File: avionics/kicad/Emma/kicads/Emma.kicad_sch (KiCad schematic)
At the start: 74 parts, among them U1 ByA 100nF +3V3 U1-VDDA Bypass, U1 ByB 100nF +3V3 U1-VDD Bypass

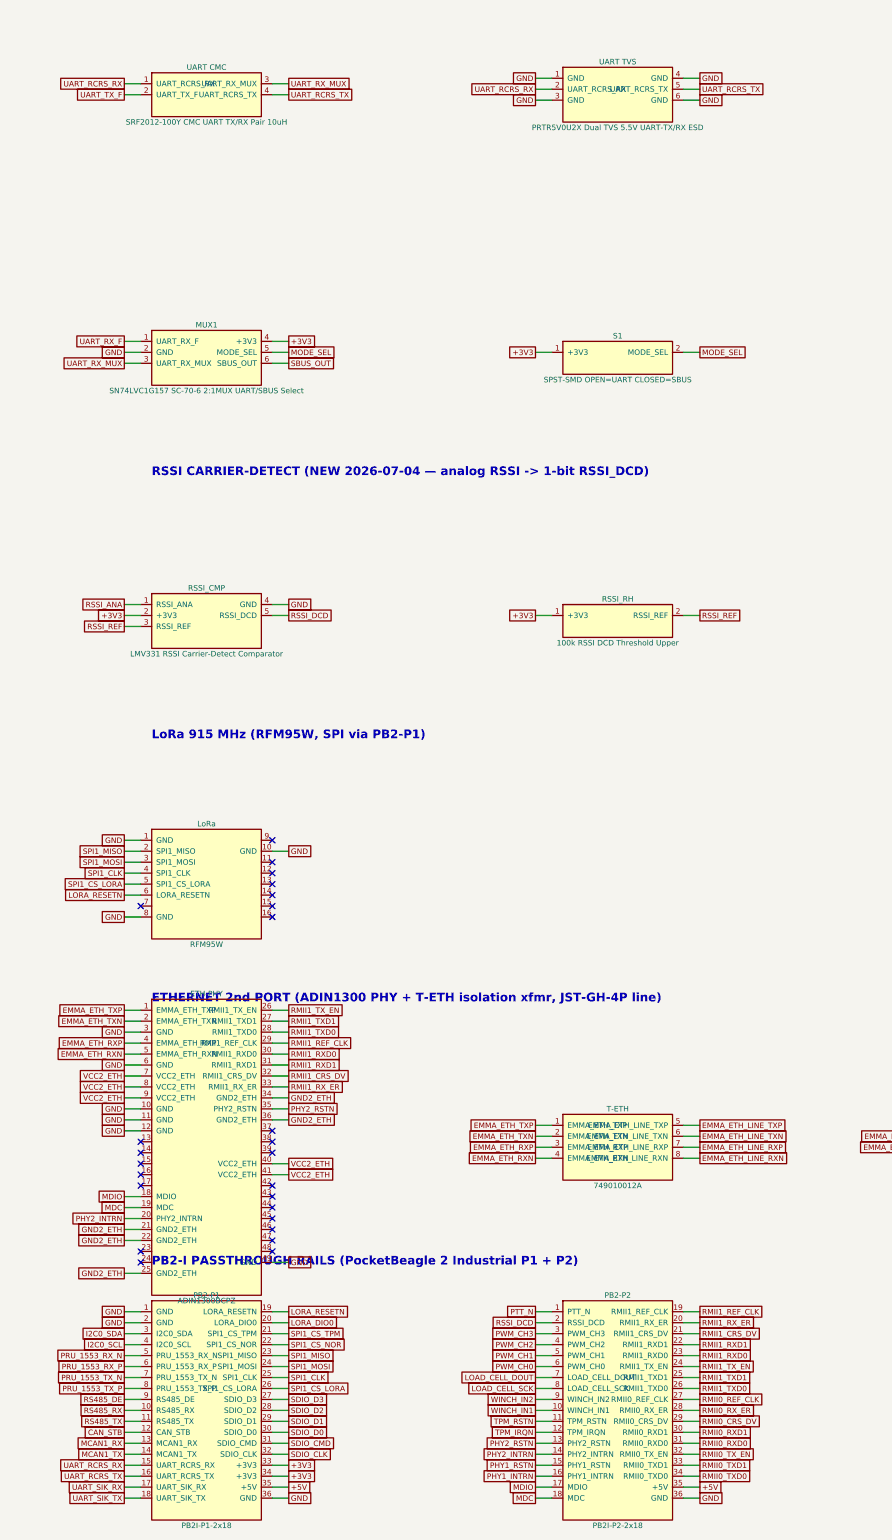
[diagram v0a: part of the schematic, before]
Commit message: Resolve TODO 0.1: rename RCRS code identifiers to 49MHZ_XCVR/XCVR-49MHZ
Code (net labels, C macros, connector/config identifiers) previously used
"RCRS" as a naming convention under the mistaken assumption the 49 MHz
link falls under FCC Part 95 Radio Control Radio Service. It's actually
governed by 47 CFR Part 15 §15.235 (REF-FCC-003) -- Part 95 was evaluated
and rejected (REF-FCC-004). User-approved rename target is frequency-
qualified "49MHZ_XCVR"/"XCVR-49MHZ" to avoid ambiguity with "Emma," the
board name that also carries LoRa.

Renamed: SI5351_RCRS_*/si5351_set_rcrs_channel() and MAL_RCRS_* firmware
macros; UART_RCRS_TX/RX KiCad net labels in the Zoe/Emma schematics and
PCBs (pure net-name text substitution, occurrence counts verified 1:1,
no geometry/placement/routing touched) and their generator scripts;
RCRS-49/TVS-RCRS/FB-RCRS component naming in Emma.md/Zoe.md and the
active current-specification files; a DTS pinctrl label and a malcolm
config key.

While auditing, also found and corrected a stale/incorrect citation in
the Cape-B-2 DTS overlay and in serenity-rev-r.jsx that still cited
"47 CFR Part 95 ... RCRS" as the governing regulation for the 49 MHz
channel plan -- the exact claim REFERENCES.md's REF-FCC-003 documents
as superseded everywhere else. Corrected to cite Part 15 Section 15.235.

Left unchanged: legitimate regulatory-term uses of "RCRS" (correctly
discussing the real FCC Part 95 RCRS designation for comparison/
rejection purposes); dated historical WBS log entries; already-archived
BOM snapshots that self-document the same correction via strikethrough;
Gerber fab output (net-name text is informational, doesn't affect the
physical board); the rcrs49_wire_post.scad filename itself (a physical-
file rename touching 7+ cross-references is separate, larger work).

ERC/DRC could not be re-verified in this environment: tools/validate_kicad.py
requires KiCad >=8 (sch erc/pcb drc CLI subcommands); only KiCad 7.0.11
was installable here (both the Ki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
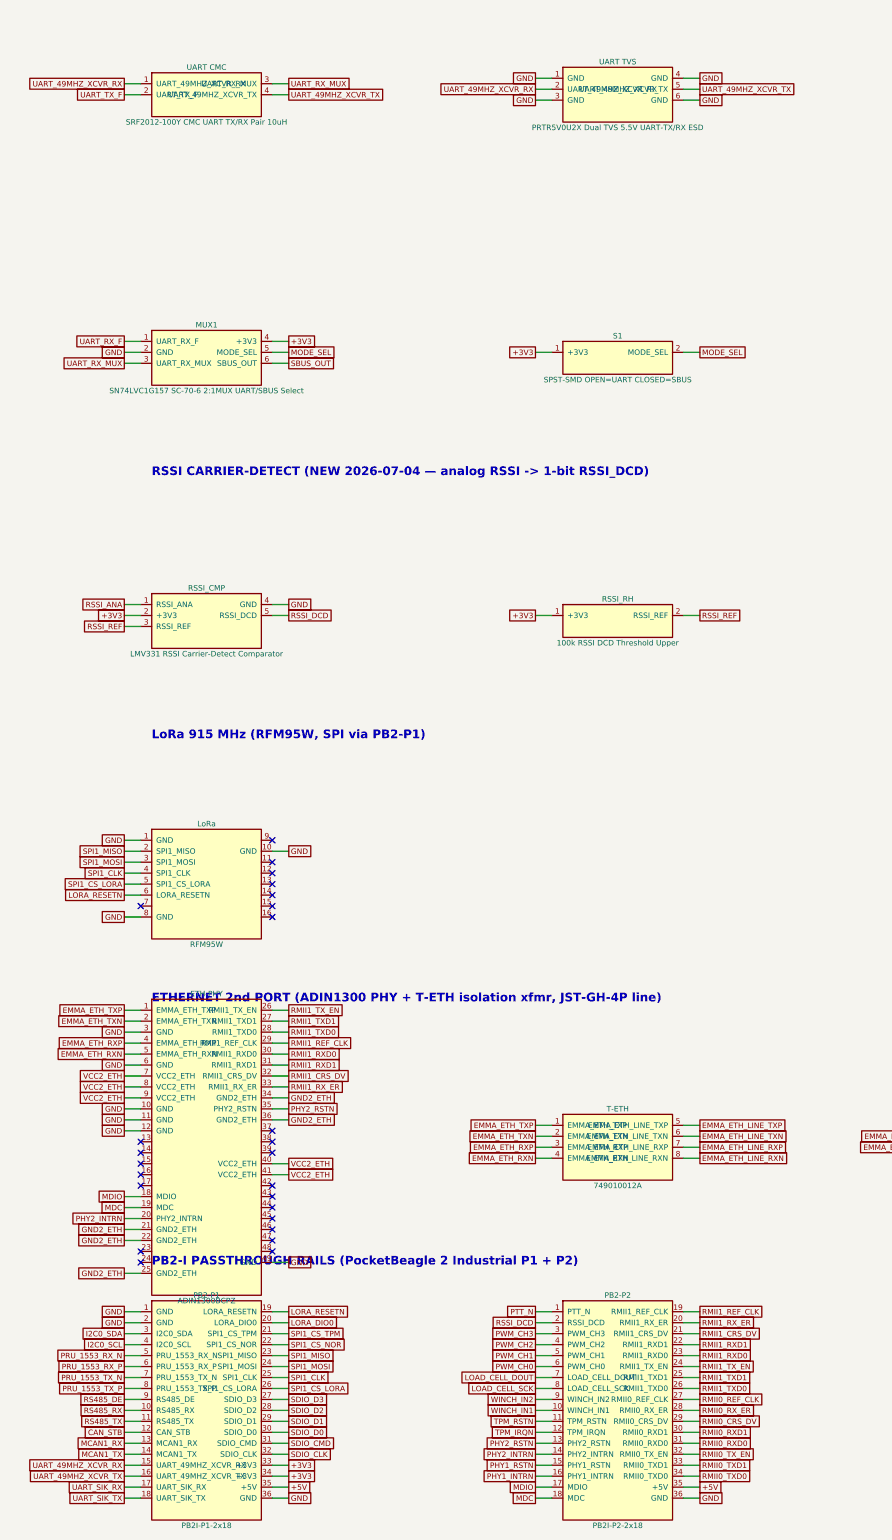
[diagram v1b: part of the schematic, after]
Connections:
- net UART_RCRS_RX renamed UART_49MHZ_XCVR_RX
- net UART_RCRS_TX renamed UART_49MHZ_XCVR_TX
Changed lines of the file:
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@@
   )
   (wire (pts (xy 48.26 731.52) (xy 44.45 731.52)) (stroke (width 0) (type default)))
-  (global_label "UART_RCRS_RX" (shape passive) (at 44.45 731.52 180) (effects (font (size 1.27 1.27)) (justify right)))
+  (global_label "UART_49MHZ_XCVR_RX" (shape passive) (at 44.45 731.52 180) (effects (font (size 1.27 1.27)) (justify right)))
   (wire (pts (xy 48.26 734.06) (xy 44.45 734.06)) (stroke (width 0) (type default)))
   (global_label "UART_TX_F" (shape passive) (at 44.45 734.06 180) (effects (font (size 1.27 1.27)) (justify right)))
@@
   (global_label "UART_RX_MUX" (shape passive) (at 82.55 731.52 0) (effects (font (size 1.27 1.27)) (justify left)))
   (wire (pts (xy 78.74 734.06) (xy 82.55 734.06)) (stroke (width 0) (type default)))
-  (global_label "UART_RCRS_TX" (shape passive) (at 82.55 734.06 0) (effects (font (size 1.27 1.27)) (justify left)))
+  (global_label "UART_49MHZ_XCVR_TX" (shape passive) (at 82.55 734.06 0) (effects (font (size 1.27 1.27)) (justify left)))
   (symbol (lib_id "S_UART_TVS") (at 158.75 734.06 0) (unit 1)
     (exclude_from_sim no) (in_bom yes) (on_board yes) (dnp no)
@@
   (global_label "GND" (shape passive) (at 139.70 730.25 180) (effects (font (size 1.27 1.27)) (justify right)))
   (wire (pts (xy 143.51 732.79) (xy 139.70 732.79)) (stroke (width 0) (type default)))
-  (global_label "UART_RCRS_RX" (shape passive) (at 139.70 732.79 180) (effects (font (size 1.27 1.27)) (justify right)))
+  (global_label "UART_49MHZ_XCVR_RX" (shape passive) (at 139.70 732.79 180) (effects (font (size 1.27 1.27)) (justify right)))
   (wire (pts (xy 143.51 735.33) (xy 139.70 735.33)) (stroke (width 0) (type default)))
   (global_label "GND" (shape passive) (at 139.70 735.33 180) (effects (font (size 1.27 1.27)) (justify right)))
@@
   (global_label "GND" (shape passive) (at 177.80 730.25 0) (effects (font (size 1.27 1.27)) (justify left)))
   (wire (pts (xy 173.99 732.79) (xy 177.80 732.79)) (stroke (width 0) (type default)))
-  (global_label "UART_RCRS_TX" (shape passive) (at 177.80 732.79 0) (effects (font (size 1.27 1.27)) (justify left)))
+  (global_label "UART_49MHZ_XCVR_TX" (shape passive) (at 177.80 732.79 0) (effects (font (size 1.27 1.27)) (justify left)))
   (wire (pts (xy 173.99 735.33) (xy 177.80 735.33)) (stroke (width 0) (type default)))
   (global_label "GND" (shape passive) (at 177.80 735.33 0) (effects (font (size 1.27 1.27)) (justify left)))
@@
   (global_label "MCAN1_TX" (shape passive) (at 44.45 1049.02 180) (effects (font (size 1.27 1.27)) (justify right)))
   (wire (pts (xy 48.26 1051.56) (xy 44.45 1051.56)) (stroke (width 0) (type default)))
-  (global_label "UART_RCRS_RX" (shape passive) (at 44.45 1051.56 180) (effects (font (size 1.27 1.27)) (justify right)))
+  (global_label "UART_49MHZ_XCVR_RX" (shape passive) (at 44.45 1051.56 180) (effects (font (size 1.27 1.27)) (justify right)))
   (wire (pts (xy 48.26 1054.10) (xy 44.45 1054.10)) (stroke (width 0) (type default)))
-  (global_label "UART_RCRS_TX" (shape passive) (at 44.45 1054.10 180) (effects (font (size 1.27 1.27)) (justify right)))
+  (global_label "UART_49MHZ_XCVR_TX" (shape passive) (at 44.45 1054.10 180) (effects (font (size 1.27 1.27)) (justify right)))
   (wire (pts (xy 48.26 1056.64) (xy 44.45 1056.64)) (stroke (width 0) (type default)))
   (global_label "UART_SIK_RX" (shape passive) (at 44.45 1056.64 180) (effects (font (size 1.27 1.27)) (justify right)))

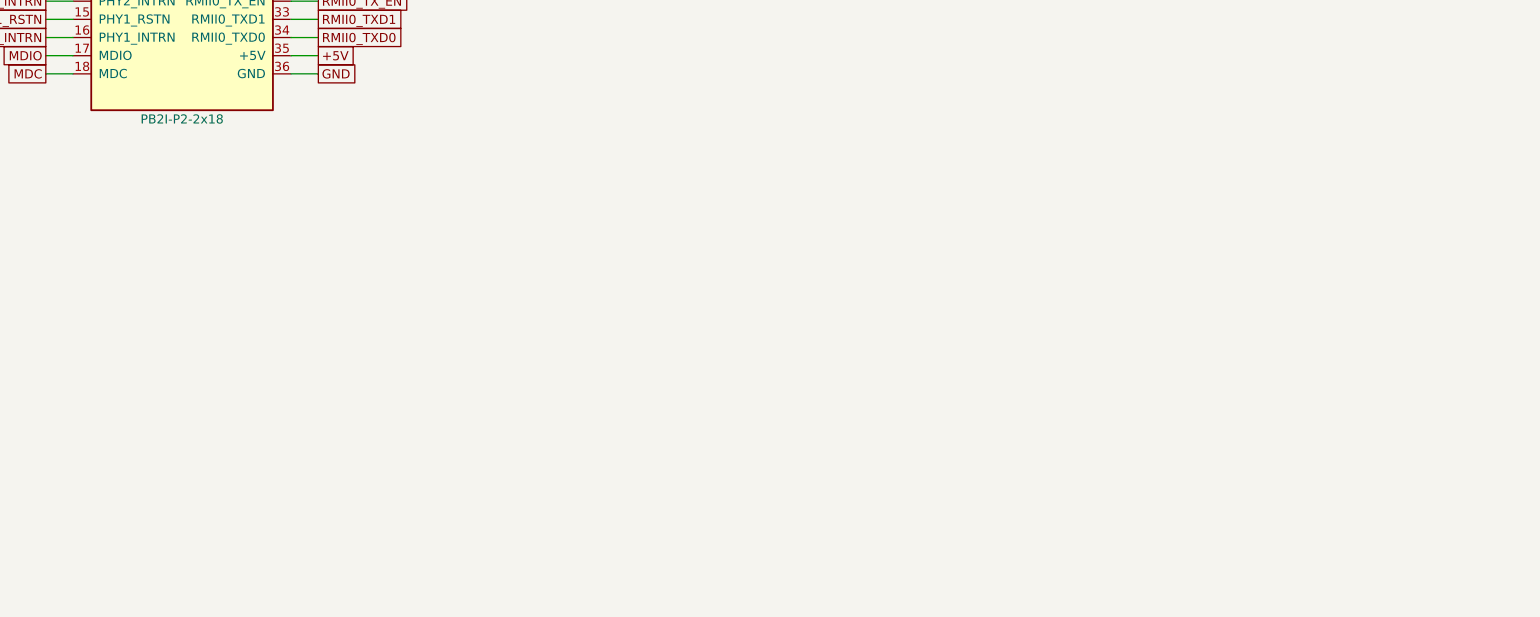
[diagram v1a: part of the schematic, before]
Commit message: Fleet trust module (MCU+TPM+isolated CAN-FD+RS-485) across new CAN-PERIPH-GW-1 board, Jayne, Kaylee, Emma; ISOW1412 swap on Wash/Zoë
- New stackable CAN-PERIPH-GW-1 gateway board (N_STACKS param): MSPM0G3507
  + SLB9670 TPM + ISOW1044BDFMR isolated CAN-FD + ISOW1412 isolated RS-485,
  informed by the public VimDrones ap_periph_pico/ESC S50 concept (no
  VimDrones GPL-3.0 source copied). PCB freerouted via the Specctra DSN/SES
  bridge (tools/export-specctra-dsn.py + import-specctra-ses.py +
  freerouting 2.2.4); user's manual footprint packing preserved.
- Jayne: added ISOW1412 isolated RS-485 (Section H); MSPM0G3507 pinmux
  re-verified against the real datasheet for all new assignments.
- Kaylee: full trust module added via non-destructive schematic injection
  (inject_kaylee_trust_module.py) -- gen_kaylee.py itself has drifted from
  the checked-in file and is not safe to regenerate from (tracked as an
  open item).
- Emma: SLB9670 TPM added via a dedicated header (inject_emma_tpm.py); no
  separate CAN/RS-485 needed, reaches the bus via Zoë's P1/P2 link.
- Fleet-wide ADM2795E -> ISOW1412 (integrated isolated DC-DC). While
  swapping Wash/Zoë, fixed their pre-existing broken ADM2795EBRWZ pin
  numbering and wrong ISOW1044BDFMR footprint (SOIC-16W on a 20-pin part).
- REFERENCES.md: REF-SENSOR-009/010/011 (ISOW1044/ISOW1412/SLB9670),
  ADM2795E supersession, Wash/Zoë defect history, vimdrones GPL note.
- WBS/TODO updated across avionics, airframe/wings-nacelles, and root:
  AK7455 nacelle tilt data is now bus-published by the gateway rather than
  read directly by River/Simon.

Co-Authored-By: Claude Sonnet 5 <noreply@anthropic.com>
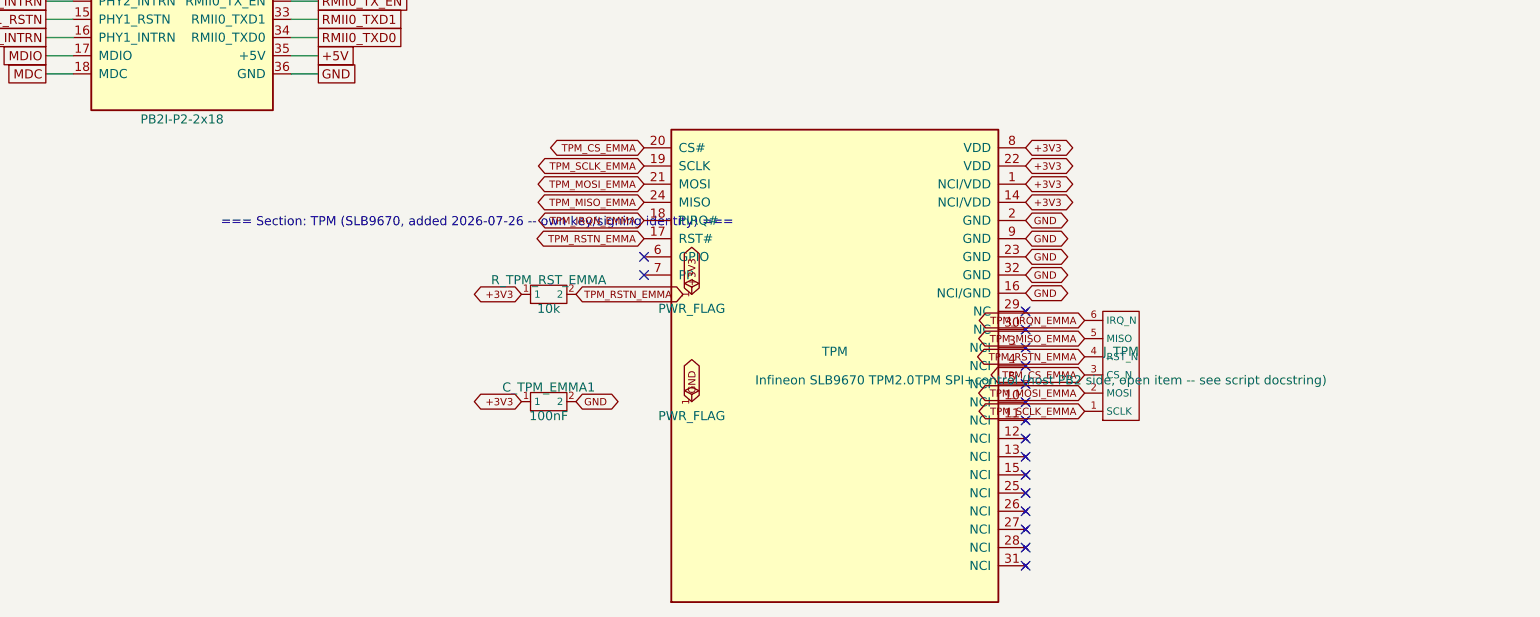
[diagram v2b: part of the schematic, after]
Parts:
- added C_TPM_EMMA1: 100nF, Capacitor_SMD:C_0402_1005Metric, symbol C_Generic_TPM
- added J_TPM: TPM SPI+control (host PB2 side, open item -- see 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, Connector_PinHeader_2.54mm:PinHeader_1x06_P2.54mm_Vertical, symbol J_TPM_EMMA
- added R_TPM_RST_EMMA: 10k, Resistor_SMD:R_0402_1005Metric, symbol R_Generic_TPM
- added TPM: Infineon SLB9670 TPM2.0, Package_DFN_QFN:QFN-32-1EP_5x5mm_P0.5mm_EP3.45x3.45mm, symbol Jayne_SLB9670_TPM
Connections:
- net +3V3: now also C_TPM_EMMA1.1, R_TPM_RST_EMMA.1, TPM.1 (NCI/VDD), TPM.14 (NCI/VDD), TPM.22 (VDD), TPM.8 (VDD)
- net GND: now also C_TPM_EMMA1.2, TPM.16 (NCI/GND), TPM.2 (GND), TPM.23 (GND), TPM.32 (GND), TPM.9 (GND)
- new net TPM_CS_EMMA: J_TPM.3 (CS_N), TPM.20 (CS#)
- new net TPM_IRQN_EMMA: J_TPM.6 (IRQ_N), TPM.18 (PIRQ#)
- new net TPM_MISO_EMMA: J_TPM.5 (MISO), TPM.24 (MISO)
- new net TPM_MOSI_EMMA: J_TPM.2 (MOSI), TPM.21 (MOSI)
- new net TPM_RSTN_EMMA: J_TPM.4 (RST_N), R_TPM_RST_EMMA.2, TPM.17 (RST#)
- new net TPM_SCLK_EMMA: J_TPM.1 (SCLK), TPM.19 (SCLK)
- no-connect marks 26 -> 43
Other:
- note added: "=== Section: TPM (SLB9670, added 2026-07-26 -- own key/signing identity) ==="
